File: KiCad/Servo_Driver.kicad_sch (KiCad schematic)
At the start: 32 parts, among them J1 2Cell, J2 Servo_1, J3 Servo_2, J4 SIGNAL_INPUT, SW1 PWM1_SW, SW2 PWM2_SW, SW3 RST_SW, SW4 CENTER_SW, SW5 EN1_SW, SW6 EN2_SW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

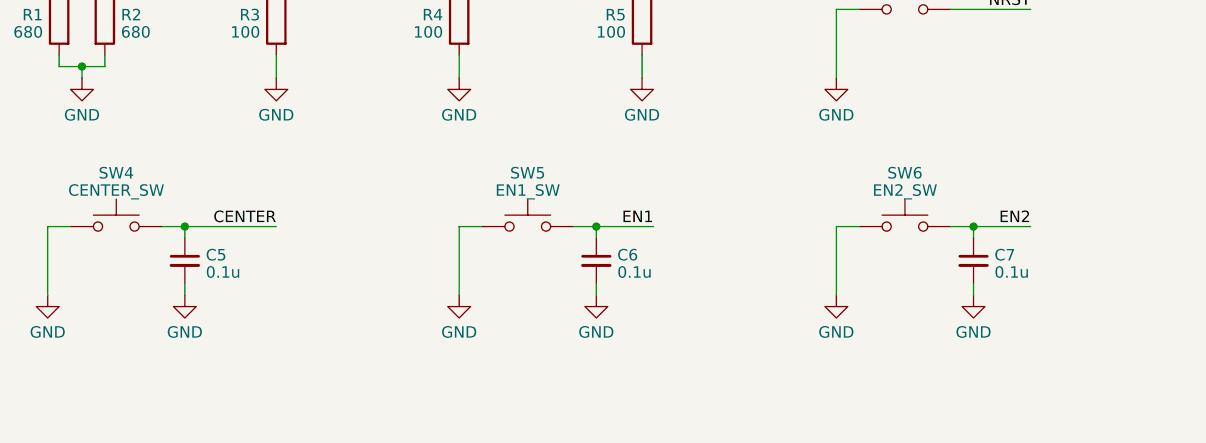
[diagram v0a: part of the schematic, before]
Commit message: 基板を更新。部品配置の変更とフットプリントの配置
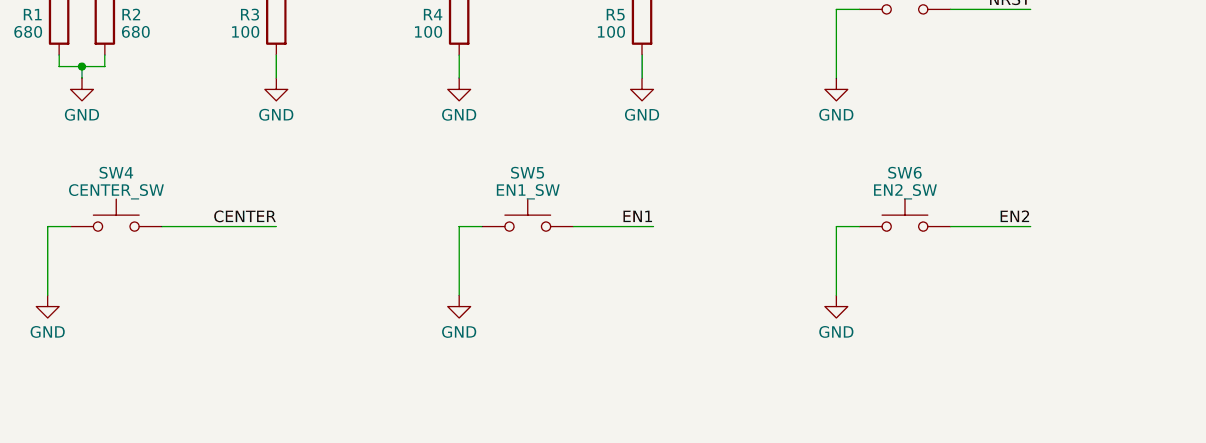
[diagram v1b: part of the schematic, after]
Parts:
- removed C5, C6, C7: 0.1u, Capacitor_THT:C_Disc_D4.3mm_W1.9mm_P5.00mm, symbol Device:C_Small
